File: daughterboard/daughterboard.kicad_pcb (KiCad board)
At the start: 2 copper layers, 40 x 55.9 mm, 40 parts, among them CON1 12V_JACK, IC1 ATMEGA328P-A, P1 X_PB01, P2 X_PC1, P3 CONN_13X2, P4 AZIMUTH, P5 ELEVATION, P6 X_ADC67, P7 VALVE, P8 X_PD4567, Q1 TIP120, U1 ULN2803A, Y1 8MHz

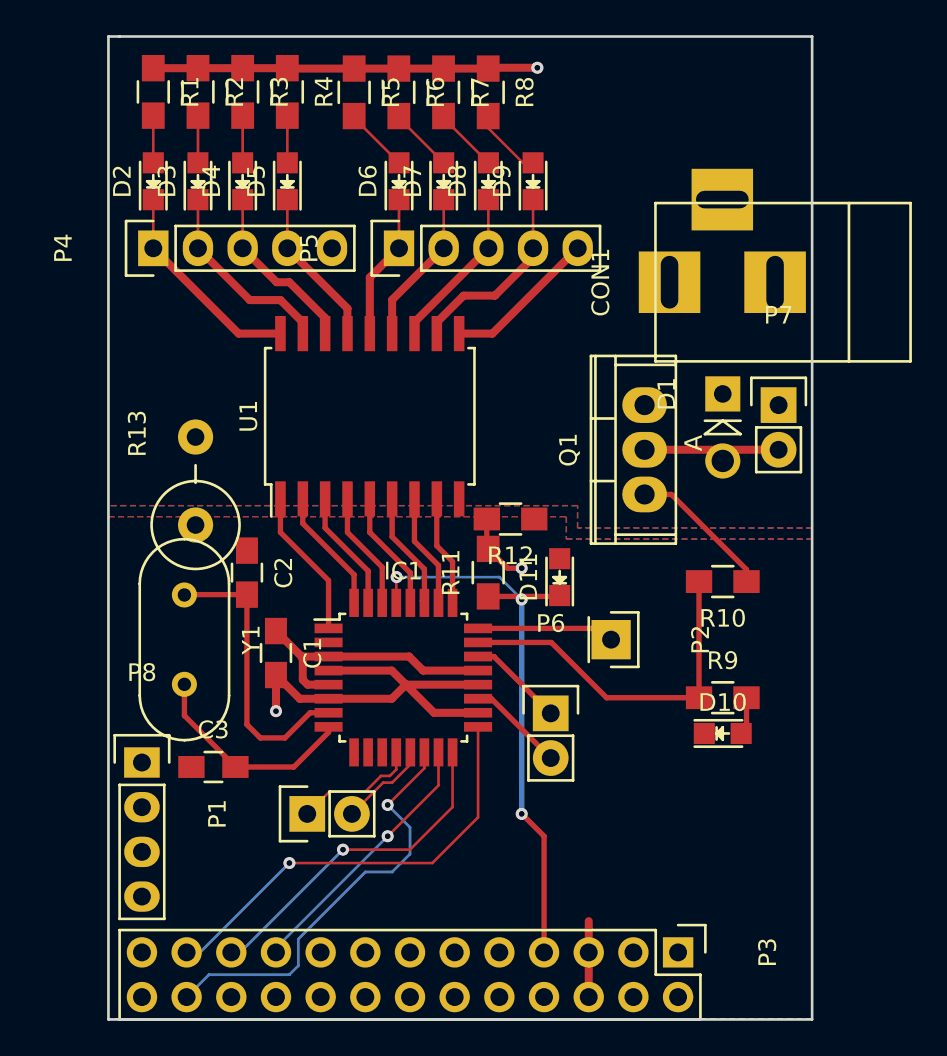
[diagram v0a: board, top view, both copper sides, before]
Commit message: Tweak footprint for barrel jack, move unused port off board / tweak trace
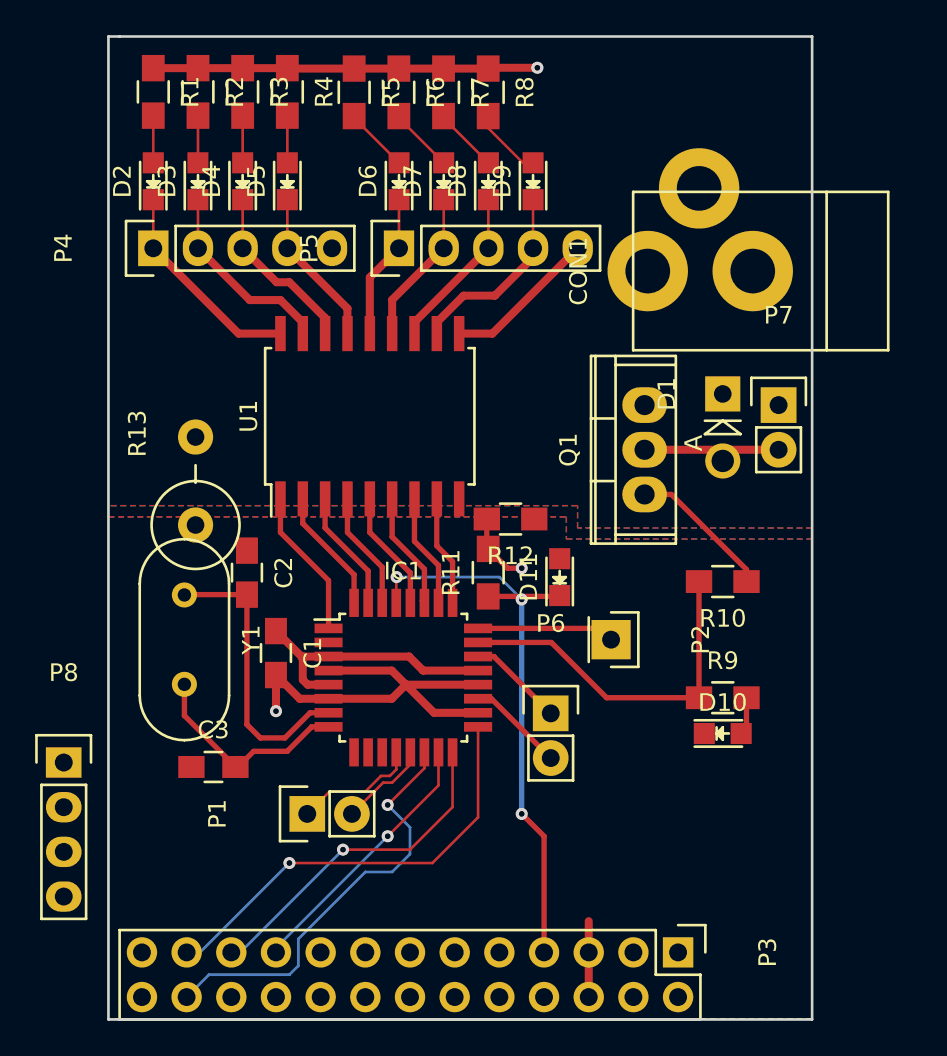
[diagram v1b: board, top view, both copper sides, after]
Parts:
- CON1: footprint Connect:BARREL_JACK -> footprints:BARREL_JACK
- moved P8 4.45 mm to (140.3, 166.4)
- moved CON1 1.42 mm to (179.7, 138.5)
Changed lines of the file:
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@@
     (links 92)
     (no_connects 7)
-    (area 127.606667 112.000001 242.964763 187.88)
+    (area 142.789999 125.044999 182.945001 181.075001)
     (thickness 1.6)
     (drawings 39)
-    (tracks 195)
+    (tracks 197)
     (zones 0)
     (modules 40)
@@
     )
   )
-  (module Connect:BARREL_JACK (layer F.Cu)
-    (at 180.965 139.09 180)
-    (descr "DC Barrel Jack")
-    (tags "Power Jack")
-    (fp_text reference CON1 (at 10.09904 0 270) (layer F.SilkS)
-      (effects (font (size 1 1) (thickness 0.15)))
-    )
-    (fp_text value 12V_JACK (at -2.54 0 450) (layer F.Fab)
-      (effects (font (size 1 1) (thickness 0.15)))
-    )
-    (fp_line (start -4.0005 -4.50088) (end -4.0005 4.50088) (layer F.SilkS) (width 0.15))
-    (fp_line (start -7.50062 -4.50088) (end -7.50062 4.50088) (layer F.SilkS) (width 0.15))
-    (fp_line (start -7.50062 4.50088) (end 7.00024 4.50088) (layer F.SilkS) (width 0.15))
-    (fp_line (start 7.00024 4.50088) (end 7.00024 -4.50088) (layer F.SilkS) (width 0.15))
-    (fp_line (start 7.00024 -4.50088) (end -7.50062 -4.50088) (layer F.SilkS) (width 0.15))
-    (pad 1 thru_hole rect (at 6.20014 0 180) (size 3.50012 3.50012) (drill oval 1.00076 2.99974) (layers *.Cu *.Mask F.SilkS)
-      (net 6 +12V))
-    (pad 2 thru_hole rect (at 0.20066 0 180) (size 3.50012 3.50012) (drill oval 1.00076 2.99974) (layers *.Cu *.Mask F.SilkS)
-      (net 1 GND))
-    (pad 3 thru_hole rect (at 3.2004 4.699 180) (size 3.50012 3.50012) (drill oval 2.99974 1.00076) (layers *.Cu *.Mask F.SilkS)
-      (net 1 GND))
-  )
   (module Diodes_ThroughHole:Diode_DO-41_SOD81_Vertical_AnodeUp (layer F.Cu)
     (at 177.79 145.44 270)
@@
   )
   (module Pin_Headers:Pin_Header_Straight_1x04 (layer F.Cu)
-    (at 144.77 166.395)
+    (at 140.325 166.395)
     (descr "Through hole pin header")
     (tags "pin header")
@@
       (net 2 GNDD))
     (pad 2 thru_hole circle (at 2.5019 0 90) (size 1.99898 1.99898) (drill 1.00076) (layers *.Cu *.SilkS *.Mask)
+      (net 1 GND))
+  )
+  (module footprints:BARREL_JACK (layer F.Cu)
+    (at 179.695 138.455 180)
+    (descr "DC Barrel Jack")
+    (tags "Power Jack")
+    (fp_text reference CON1 (at 10.09904 0 270) (layer F.SilkS)
+      (effects (font (size 1 1) (thickness 0.15)))
+    )
+    (fp_text value 12V_JACK (at -2.54 0 450) (layer F.Fab)
+      (effects (font (size 1 1) (thickness 0.15)))
+    )
+    (fp_line (start -4.0005 -4.50088) (end -4.0005 4.50088) (layer F.SilkS) (width 0.15))
+    (fp_line (start -7.50062 -4.50088) (end -7.50062 4.50088) (layer F.SilkS) (width 0.15))
+    (fp_line (start -7.50062 4.50088) (end 7.00024 4.50088) (layer F.SilkS) (width 0.15))
+    (fp_line (start 7.00024 4.50088) (end 7.00024 -4.50088) (layer F.SilkS) (width 0.15))
+    (fp_line (start 7.00024 -4.50088) (end -7.50062 -4.50088) (layer F.SilkS) (width 0.15))
+    (pad 3 thru_hole circle (at 3.24866 4.699 180) (size 4.572 4.572) (drill 2.54) (layers *.Cu *.Mask F.SilkS)
+      (net 1 GND))
+    (pad 1 thru_hole circle (at 6.16966 0 180) (size 4.572 4.572) (drill 2.54) (layers *.Cu *.Mask F.SilkS)
+      (net 6 +12V))
+    (pad 2 thru_hole circle (at 0.20066 0 180) (size 4.572 4.572) (drill 2.54) (layers *.Cu *.Mask F.SilkS)
       (net 1 GND))
   )
@@
   (segment (start 152.898 164.998) (end 151.501 164.998) (width 0.3048) (layer F.Cu) (net 4))
   (segment (start 154.327 163.569) (end 152.898 164.998) (width 0.3048) (layer F.Cu) (net 4))
+  (segment (start 155.379 164.369) (end 154.416 164.369) (width 0.3048) (layer F.Cu) (net 5))
+  (segment (start 151.12 165.76) (end 150.231 166.649) (width 0.3048) (layer F.Cu) (net 5))
+  (segment (start 153.025 165.76) (end 151.12 165.76) (width 0.3048) (layer F.Cu) (net 5))
+  (segment (start 154.416 164.369) (end 153.025 165.76) (width 0.3048) (layer F.Cu) (net 5))
+  (segment (start 150.231 166.649) (end 150.084 166.649) (width 0.3048) (layer F.Cu) (net 5))
   (segment (start 150.084 166.649) (end 150.084 166.629) (width 0.3048) (layer F.Cu) (net 5))
   (segment (start 150.084 166.629) (end 147.183 163.728) (width 0.3048) (layer F.Cu) (net 5))
   (segment (start 147.183 163.728) (end 147.183 161.95) (width 0.3048) (layer F.Cu) (net 5))
-  (segment (start 155.379 164.369) (end 155.379 164.676) (width 0.3048) (layer F.Cu) (net 5))
-  (segment (start 153.406 166.649) (end 150.084 166.649) (width 0.3048) (layer F.Cu) (net 5))
-  (segment (start 155.379 164.676) (end 153.406 166.649) (width 0.3048) (layer F.Cu) (net 5))
   (segment (start 162.804 142.01) (end 164.695 142.01) (width 0.4572) (layer F.Cu) (net 6))
   (segment (start 164.695 142.01) (end 169.545 137.16) (width 0.4572) (layer F.Cu) (net 6))

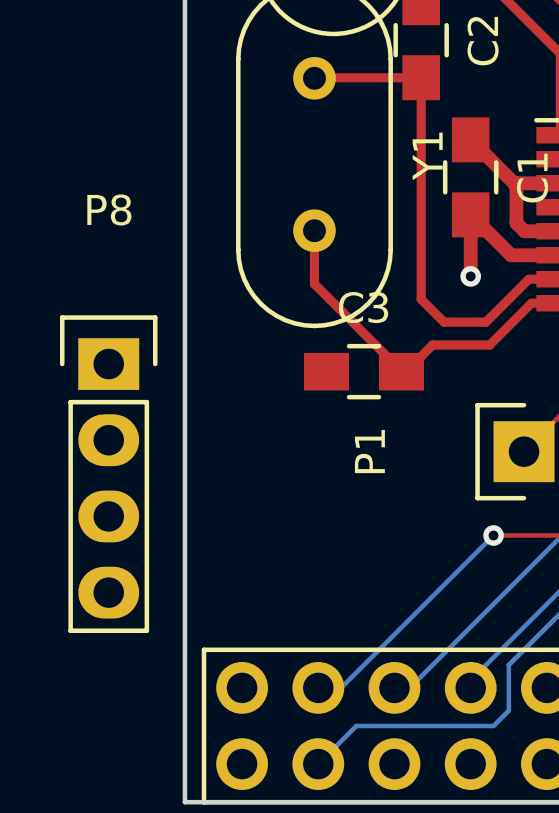
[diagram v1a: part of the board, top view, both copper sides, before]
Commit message: Remove unused header from PCB
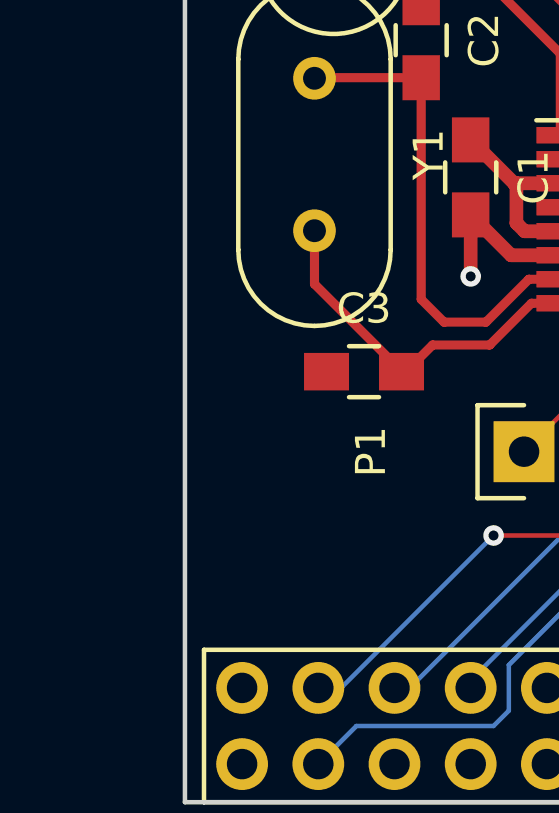
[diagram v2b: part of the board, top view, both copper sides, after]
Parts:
- removed P8: X_PD4567, Pin_Headers:Pin_Header_Straight_1x04
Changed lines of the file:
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@@
 (kicad_pcb (version 4) (host pcbnew 4.0.2+dfsg1-stable)
   (general
-    (links 92)
-    (no_connects 7)
+    (links 88)
+    (no_connects 3)
     (area 142.789999 125.044999 182.945001 181.075001)
     (thickness 1.6)
@@
     (tracks 197)
     (zones 0)
-    (modules 40)
+    (modules 39)
     (nets 50)
   )
@@
       (scale (xyz 1 1 1))
       (rotate (xyz 0 0 90))
-    )
-  )
-  (module Pin_Headers:Pin_Header_Straight_1x04 (layer F.Cu)
-    (at 140.325 166.395)
-    (descr "Through hole pin header")
-    (tags "pin header")
-    (fp_text reference P8 (at 0 -5.1) (layer F.SilkS)
-      (effects (font (size 1 1) (thickness 0.15)))
-    )
-    (fp_text value X_PD4567 (at 2.032 4.191 90) (layer F.Fab)
-      (effects (font (size 1 1) (thickness 0.15)))
-    )
-    (fp_line (start -1.75 -1.75) (end -1.75 9.4) (layer F.CrtYd) (width 0.05))
-    (fp_line (start 1.75 -1.75) (end 1.75 9.4) (layer F.CrtYd) (width 0.05))
-    (fp_line (start -1.75 -1.75) (end 1.75 -1.75) (layer F.CrtYd) (width 0.05))
-    (fp_line (start -1.75 9.4) (end 1.75 9.4) (layer F.CrtYd) (width 0.05))
-    (fp_line (start -1.27 1.27) (end -1.27 8.89) (layer F.SilkS) (width 0.15))
-    (fp_line (start 1.27 1.27) (end 1.27 8.89) (layer F.SilkS) (width 0.15))
-    (fp_line (start 1.55 -1.55) (end 1.55 0) (layer F.SilkS) (width 0.15))
-    (fp_line (start -1.27 8.89) (end 1.27 8.89) (layer F.SilkS) (width 0.15))
-    (fp_line (start 1.27 1.27) (end -1.27 1.27) (layer F.SilkS) (width 0.15))
-    (fp_line (start -1.55 0) (end -1.55 -1.55) (layer F.SilkS) (width 0.15))
-    (fp_line (start -1.55 -1.55) (end 1.55 -1.55) (layer F.SilkS) (width 0.15))
-    (pad 1 thru_hole rect (at 0 0) (size 2.032 1.7272) (drill 1.016) (layers *.Cu *.Mask F.SilkS)
-      (net 24 "Net-(IC1-Pad2)"))
-    (pad 2 thru_hole oval (at 0 2.54) (size 2.032 1.7272) (drill 1.016) (layers *.Cu *.Mask F.SilkS)
-      (net 25 "Net-(IC1-Pad9)"))
-    (pad 3 thru_hole oval (at 0 5.08) (size 2.032 1.7272) (drill 1.016) (layers *.Cu *.Mask F.SilkS)
-      (net 26 "Net-(IC1-Pad10)"))
-    (pad 4 thru_hole oval (at 0 7.62) (size 2.032 1.7272) (drill 1.016) (layers *.Cu *.Mask F.SilkS)
-      (net 27 "Net-(IC1-Pad11)"))
-    (model Pin_Headers.3dshapes/Pin_Header_Straight_1x04.wrl
-      (at (xyz 0 -0.15 0))
-      (scale (xyz 1 1 1))
-      (rotate (xyz 0 0 90))
